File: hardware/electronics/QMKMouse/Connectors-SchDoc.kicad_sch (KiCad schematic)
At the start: 19 parts

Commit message: update schematic from PCB; sync netlist and fix some symbol orientations; also fix LED symbol
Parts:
- USB.C.19, USB.FB.1, USB.FB.2, USB.FB.3, USB.FB.4, USB.FB.5, USB.R.10, USB.R.11, USB.R.12, USB.R.13, USB.R.14, USB.R.15, USB.R.6, USB.R.7, USB.R.8, USB.R.9: footprint (none) -> Chip_Passives.PcbLib:0805
- USB.J.2: footprint (none) -> Connectors.PcbLib:SJ-43514-SMT-TR
- USB.J.3: footprint (none) -> Connectors.PcbLib:DX07S016JA1R1500
- USB.Z.1: footprint (none) -> Diodes.PcbLib:PESD3V3S4UD - SOT95P275X110-6N
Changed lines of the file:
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@@
     (property "Reference" "USB.FB.1" (id 0) (at 186.6392 82.55 90))
     (property "Value" "ACML-0805-601-T" (id 1) (at 186.6392 85.09 90))
-    (property "Footprint" "" (id 2) (at 186.69 91.948 90)
+    (property "Footprint" "Chip_Passives.PcbLib:0805" (id 2) (at 186.69 91.948 90)
       (effects (font (size 1.27 1.27)) hide)
     )
@@
     (property "Reference" "USB.FB.5" (id 0) (at 186.6392 49.53 90))
     (property "Value" "ACML-0805-601-T" (id 1) (at 186.6392 52.07 90))
-    (property "Footprint" "" (id 2) (at 186.69 58.928 90)
+    (property "Footprint" "Chip_Passives.PcbLib:0805" (id 2) (at 186.69 58.928 90)
       (effects (font (size 1.27 1.27)) hide)
     )
@@
       (effects (font (size 1.27 1.27)) (justify left))
     )
-    (property "Footprint" "" (id 2) (at 85.598 35.56 90)
+    (property "Footprint" "Chip_Passives.PcbLib:0805" (id 2) (at 85.598 35.56 90)
       (effects (font (size 1.27 1.27)) hide)
     )
@@
       (effects (font (size 1.27 1.27)) (justify left))
     )
-    (property "Footprint" "" (id 2) (at 229.87 58.928 90)
+    (property "Footprint" "Chip_Passives.PcbLib:0805" (id 2) (at 229.87 58.928 90)
       (effects (font (size 1.27 1.27)) hide)
     )
@@
       (effects (font (size 1.27 1.27)) (justify left))
     )
-    (property "Footprint" "" (id 2) (at 67.818 120.65 90)
+    (property "Footprint" "Chip_Passives.PcbLib:0805" (id 2) (at 67.818 120.65 90)
       (effects (font (size 1.27 1.27)) hide)
     )
@@
       (effects (font (size 1.27 1.27)) (justify left))
     )
-    (property "Footprint" "" (id 2) (at 95.758 120.65 90)
+    (property "Footprint" "Chip_Passives.PcbLib:0805" (id 2) (at 95.758 120.65 90)
       (effects (font (size 1.27 1.27)) hide)
     )
@@
       (effects (font (size 1.27 1.27)) (justify left))
     )
-    (property "Footprint" "" (id 2) (at 103.378 35.56 90)
+    (property "Footprint" "Chip_Passives.PcbLib:0805" (id 2) (at 103.378 35.56 90)
       (effects (font (size 1.27 1.27)) hide)
     )
@@
     (property "Reference" "USB.FB.2" (id 0) (at 186.6392 102.87 90))
     (property "Value" "ACML-0805-601-T" (id 1) (at 186.6392 105.41 90))
-    (property "Footprint" "" (id 2) (at 186.69 112.268 90)
+    (property "Footprint" "Chip_Passives.PcbLib:0805" (id 2) (at 186.69 112.268 90)
       (effects (font (size 1.27 1.27)) hide)
     )
@@
     (property "Reference" "USB.J.2" (id 0) (at 45.72 40.64 0))
     (property "Value" "SJ-43514-SMT-TR" (id 1) (at 43.18 57.15 0))
-    (property "Footprint" "" (id 2) (at 48.26 46.99 0)
+    (property "Footprint" "Connectors.PcbLib:SJ-43514-SMT-TR" (id 2) (at 48.26 46.99 0)
       (effects (font (size 1.27 1.27)) hide)
     )
@@
       (effects (font (size 1.27 1.27)) (justify left))
     )
-    (property "Footprint" "" (id 2) (at 105.918 120.65 90)
+    (property "Footprint" "Chip_Passives.PcbLib:0805" (id 2) (at 105.918 120.65 90)
       (effects (font (size 1.27 1.27)) hide)
     )
@@
       (effects (font (size 1.27 1.27)) (justify right))
     )
-    (property "Footprint" "" (id 2) (at 219.4052 90.17 0)
+    (property "Footprint" "Chip_Passives.PcbLib:0805" (id 2) (at 219.4052 90.17 0)
       (effects (font (size 1.27 1.27)) hide)
     )
@@
       (effects (font (size 1.27 1.27)) (justify right))
     )
-    (property "Footprint" "" (id 2) (at 134.62 146.05 0)
+    (property "Footprint" "Diodes.PcbLib:PESD3V3S4UD - SOT95P275X110-6N" (id 2) (at 134.62 146.05 0)
       (effects (font (size 1.27 1.27)) hide)
     )
@@
     (property "Reference" "USB.FB.4" (id 0) (at 186.6392 36.83 90))
     (property "Value" "ACML-0805-601-T Ferrite Bead 600Ohm" (id 1) (at 186.6392 39.37 90))
-    (property "Footprint" "" (id 2) (at 186.69 46.228 90)
+    (property "Footprint" "Chip_Passives.PcbLib:0805" (id 2) (at 186.69 46.228 90)
       (effects (font (size 1.27 1.27)) hide)
     )
@@
     (property "Reference" "USB.FB.3" (id 0) (at 186.6392 113.03 90))
     (property "Value" "ACML-0805-601-T" (id 1) (at 186.6392 115.57 90))
-    (property "Footprint" "" (id 2) (at 186.69 122.428 90)
+    (property "Footprint" "Chip_Passives.PcbLib:0805" (id 2) (at 186.69 122.428 90)
       (effects (font (size 1.27 1.27)) hide)
     )
@@
       (effects (font (size 1.27 1.27)) (justify left))
     )
-    (property "Footprint" "" (id 2) (at 229.87 112.268 90)
+    (property "Footprint" "Chip_Passives.PcbLib:0805" (id 2) (at 229.87 112.268 90)
       (effects (font (size 1.27 1.27)) hide)
     )
@@
       (effects (font (size 1.27 1.27)) (justify left))
     )
-    (property "Footprint" "" (id 2) (at 77.978 120.65 90)
+    (property "Footprint" "Chip_Passives.PcbLib:0805" (id 2) (at 77.978 120.65 90)
       (effects (font (size 1.27 1.27)) hide)
     )
@@
     (property "Reference" "USB.J.3" (id 0) (at 30.48 80.01 0))
     (property "Value" "DX07S016JA1R1500" (id 1) (at 30.48 82.55 0))
-    (property "Footprint" "" (id 2) (at 34.29 102.87 0)
+    (property "Footprint" "Connectors.PcbLib:DX07S016JA1R1500" (id 2) (at 34.29 102.87 0)
       (effects (font (size 1.27 1.27)) hide)
     )
@@
       (effects (font (size 1.27 1.27)) (justify left))
     )
-    (property "Footprint" "" (id 2) (at 229.87 122.428 90)
+    (property "Footprint" "Chip_Passives.PcbLib:0805" (id 2) (at 229.87 122.428 90)
       (effects (font (size 1.27 1.27)) hide)
     )
@@
       (effects (font (size 1.27 1.27)) (justify left))
     )
-    (property "Footprint" "" (id 2) (at 229.87 46.228 90)
-      (effects (font (size 1.27 1.27)) hide)
-    )
+    (property "Footprint" "Chip_Passives.PcbLib:0805" (id 2) (at 229.87 46.228 90)
+      (effects (font (size 1.27 1.27)) hide)
+    )

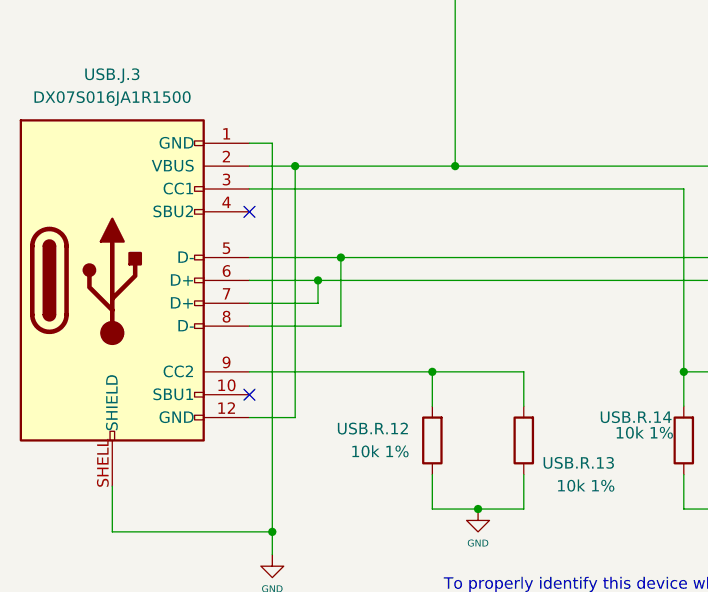
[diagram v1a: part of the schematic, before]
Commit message: Fix all remaining DRC errors and schematic mismatches
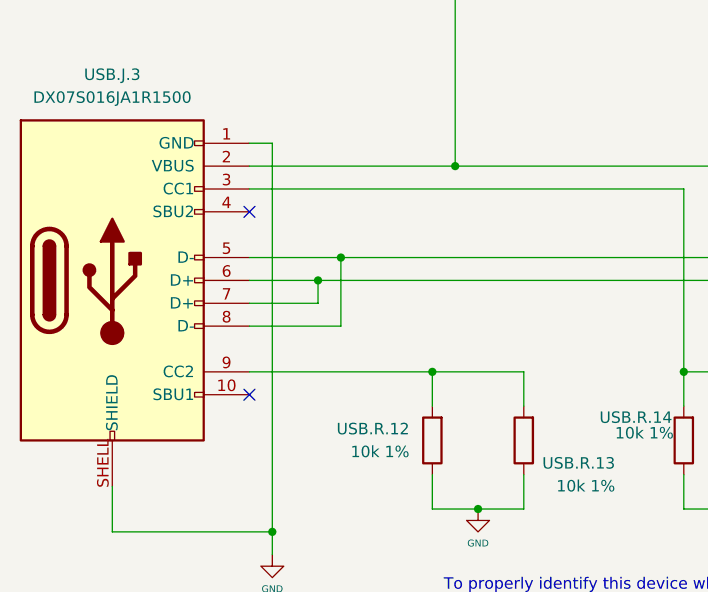
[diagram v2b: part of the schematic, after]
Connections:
- net GND: now also USB.J.3.12 (GND)
- net at USB.FB.1.1, USB.J.2.1 (S), USB.J.3.2 (VBUS)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: now also USB.J.3.11 (VBUS); no longer USB.J.3.12 (GND)
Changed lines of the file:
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@@
   (junction (at 68.58 90.17) (diameter 0) (color 0 0 0 0)
-  )
-  (junction (at 50.8 90.17) (diameter 0) (color 0 0 0 0)
   )
   (junction (at 99.06 128.27) (diameter 0) (color 0 0 0 0)
@@
     (stroke (width 0) (type default) (color 0 0 0 0))
   )
+  (wire (pts (xy 48.26 87.63) (xy 48.26 130.81))
+    (stroke (width 0) (type default) (color 0 0 0 0))
+  )
   (wire (pts (xy 104.14 116.84) (xy 104.14 113.03))
     (stroke (width 0) (type default) (color 0 0 0 0))
@@
     (stroke (width 0) (type default) (color 0 0 0 0))
   )
-  (wire (pts (xy 50.8 90.17) (xy 50.8 118.11))
-    (stroke (width 0) (type default) (color 0 0 0 0))
-  )
   (wire (pts (xy 68.58 44.45) (xy 53.34 44.45))
     (stroke (width 0) (type default) (color 0 0 0 0))
@@
     (stroke (width 0) (type default) (color 0 0 0 0))
   )
-  (wire (pts (xy 50.8 90.17) (xy 45.72 90.17))
-    (stroke (width 0) (type default) (color 0 0 0 0))
-  )
   (wire (pts (xy 167.64 166.37) (xy 167.64 113.03))
     (stroke (width 0) (type default) (color 0 0 0 0))
@@
     (stroke (width 0) (type default) (color 0 0 0 0))
   )
-  (wire (pts (xy 68.58 90.17) (xy 50.8 90.17))
+  (wire (pts (xy 45.72 90.17) (xy 68.58 90.17))
     (stroke (width 0) (type default) (color 0 0 0 0))
   )
@@
     (stroke (width 0) (type default) (color 0 0 0 0))
   )
-  (wire (pts (xy 48.26 87.63) (xy 48.26 130.81))
-    (stroke (width 0) (type default) (color 0 0 0 0))
-  )
   (wire (pts (xy 71.12 128.27) (xy 66.04 128.27))
     (stroke (width 0) (type default) (color 0 0 0 0))
@@
   )
   (wire (pts (xy 149.86 44.45) (xy 182.88 44.45))
-    (stroke (width 0) (type default) (color 0 0 0 0))
-  )
-  (wire (pts (xy 50.8 118.11) (xy 45.72 118.11))
     (stroke (width 0) (type default) (color 0 0 0 0))
   )
@@
     (pin "1")
     (pin "10")
+    (pin "11")
     (pin "12")
     (pin "2")

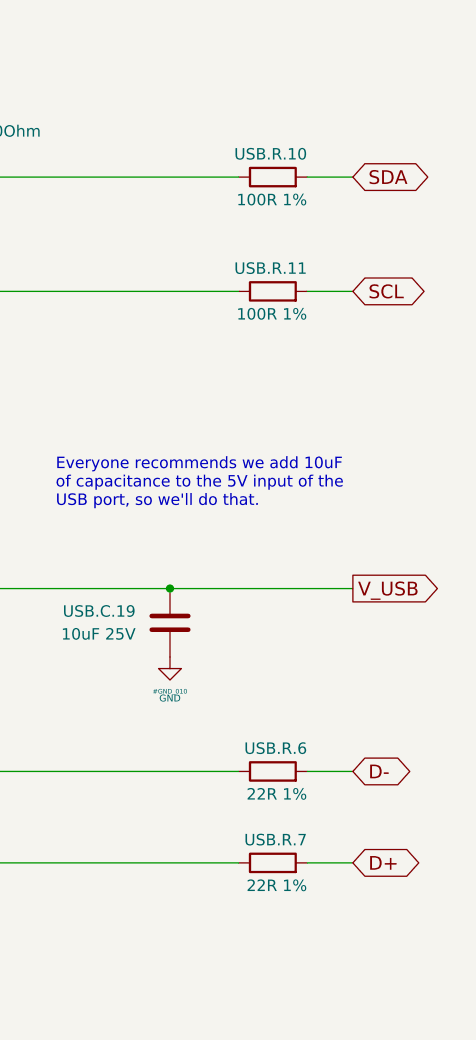
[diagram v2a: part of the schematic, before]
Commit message: fix ERC errors and use hierarchy labels
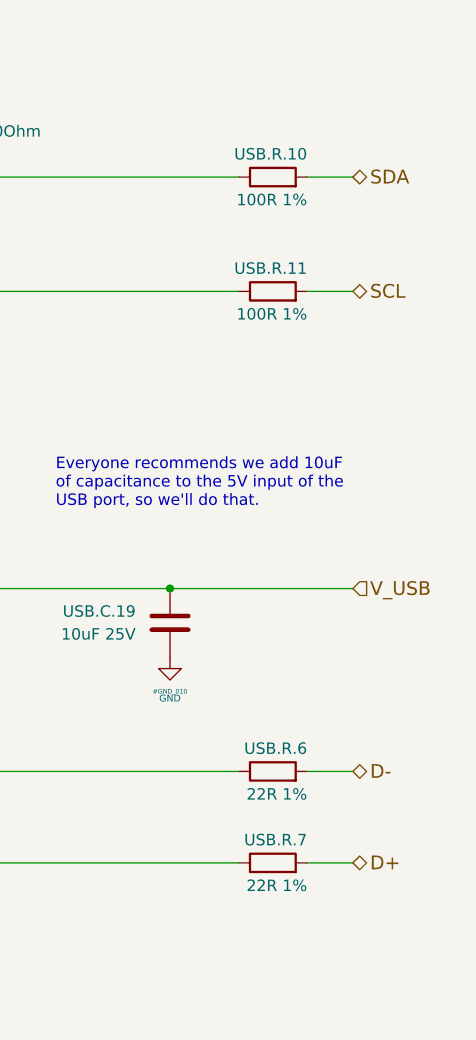
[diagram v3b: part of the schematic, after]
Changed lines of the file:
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@@
     (effects (font (size 1.27 1.27)) (justify left bottom))
   )
-  (global_label "D-" (shape bidirectional) (at 238.76 110.49 0) (fields_autoplaced)
+  (hierarchical_label "V_USB" (shape input) (at 238.76 90.17 0)
     (effects (font (size 1.524 1.524)) (justify left))
-    (property "Intersheet References" "${INTERSHEET_REFS}" (id 0) (at -7.62 -62.23 0)
-      (effects (font (size 1.27 1.27)) hide)
-    )
   )
-  (global_label "SDA" (shape bidirectional) (at 238.76 44.45 0) (fields_autoplaced)
+  (hierarchical_label "D-" (shape bidirectional) (at 238.76 110.49 0)
     (effects (font (size 1.524 1.524)) (justify left))
-    (property "Intersheet References" "${INTERSHEET_REFS}" (id 0) (at -7.62 -62.23 0)
-      (effects (font (size 1.27 1.27)) hide)
-    )
   )
-  (global_label "D+" (shape bidirectional) (at 238.76 120.65 0) (fields_autoplaced)
+  (hierarchical_label "D+" (shape bidirectional) (at 238.76 120.65 0)
     (effects (font (size 1.524 1.524)) (justify left))
-    (property "Intersheet References" "${INTERSHEET_REFS}" (id 0) (at -7.62 -62.23 0)
-      (effects (font (size 1.27 1.27)) hide)
-    )
   )
-  (global_label "V_USB" (shape output) (at 238.76 90.17 0) (fields_autoplaced)
+  (hierarchical_label "SCL" (shape bidirectional) (at 238.76 57.15 0)
     (effects (font (size 1.524 1.524)) (justify left))
-    (property "Intersheet References" "${INTERSHEET_REFS}" (id 0) (at -7.62 -62.23 0)
-      (effects (font (size 1.27 1.27)) hide)
-    )
   )
-  (global_label "SCL" (shape bidirectional) (at 238.76 57.15 0) (fields_autoplaced)
+  (hierarchical_label "SDA" (shape bidirectional) (at 238.76 44.45 0)
     (effects (font (size 1.524 1.524)) (justify left))
-    (property "Intersheet References" "${INTERSHEET_REFS}" (id 0) (at -7.62 -62.23 0)
-      (effects (font (size 1.27 1.27)) hide)
-    )
   )
   (symbol (lib_id "power:GND") (at 63.5 62.23 0) (unit 1)

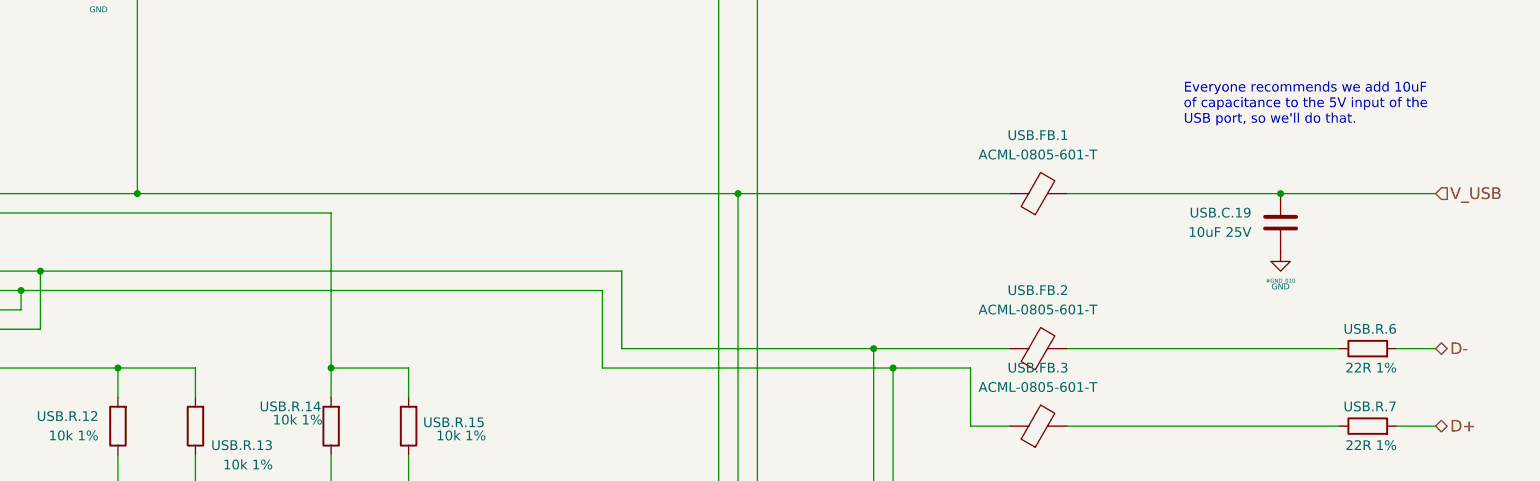
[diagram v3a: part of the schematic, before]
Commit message: Fix all ERC errors and replot the schematic
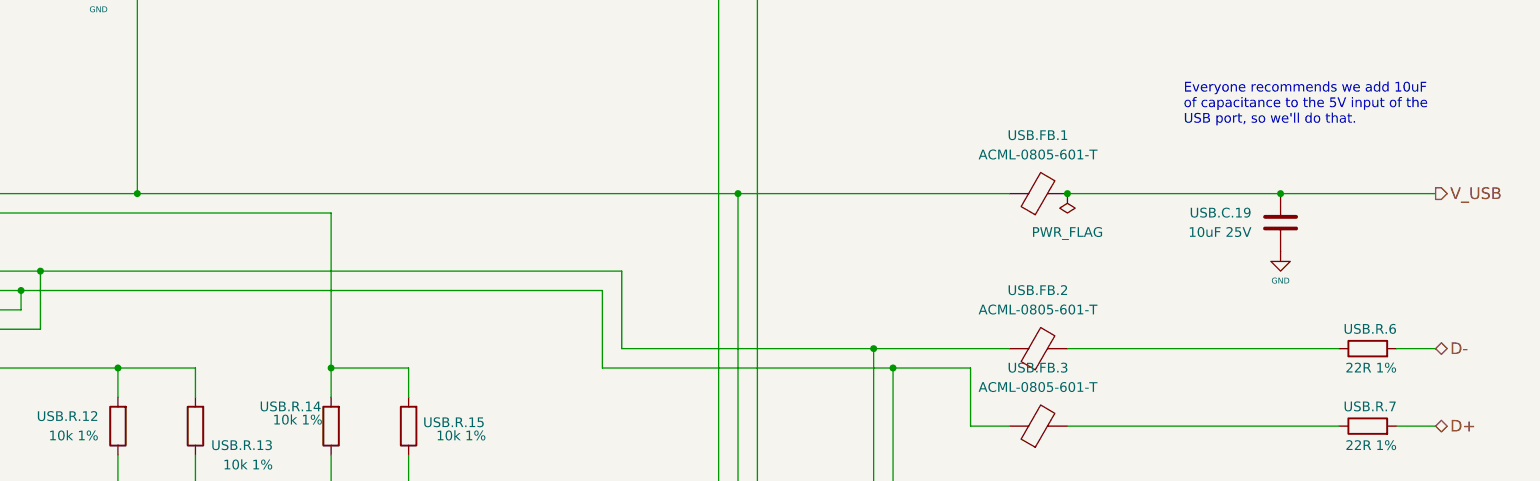
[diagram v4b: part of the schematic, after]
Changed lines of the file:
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@@
   (junction (at 93.98 113.03) (diameter 0) (color 0 0 0 0)
+  )
+  (junction (at 190.5 90.17) (diameter 0) (color 0 0 0 0)
   )
   (junction (at 167.64 113.03) (diameter 0) (color 0 0 0 0)
@@
     (stroke (width 0) (type default) (color 0 0 0 0))
   )
-  (wire (pts (xy 147.32 90.17) (xy 68.58 90.17))
-    (stroke (width 0) (type default) (color 0 0 0 0))
-  )
   (wire (pts (xy 101.6 49.53) (xy 101.6 39.37))
     (stroke (width 0) (type default) (color 0 0 0 0))
@@
     (stroke (width 0) (type default) (color 0 0 0 0))
   )
+  (wire (pts (xy 68.58 90.17) (xy 147.32 90.17))
+    (stroke (width 0) (type default) (color 0 0 0 0))
+  )
   (wire (pts (xy 165.1 156.21) (xy 165.1 110.49))
     (stroke (width 0) (type default) (color 0 0 0 0))
@@
     (stroke (width 0) (type default) (color 0 0 0 0))
   )
-  (wire (pts (xy 182.88 90.17) (xy 147.32 90.17))
-    (stroke (width 0) (type default) (color 0 0 0 0))
-  )
   (wire (pts (xy 226.06 44.45) (xy 190.5 44.45))
     (stroke (width 0) (type default) (color 0 0 0 0))
@@
   )
   (wire (pts (xy 76.2 124.46) (xy 76.2 128.27))
+    (stroke (width 0) (type default) (color 0 0 0 0))
+  )
+  (wire (pts (xy 147.32 90.17) (xy 182.88 90.17))
     (stroke (width 0) (type default) (color 0 0 0 0))
   )
@@
     (effects (font (size 1.27 1.27)) (justify left bottom))
   )
-  (hierarchical_label "V_USB" (shape input) (at 238.76 90.17 0)
+  (hierarchical_label "V_USB" (shape output) (at 238.76 90.17 0)
     (effects (font (size 1.524 1.524)) (justify left))
   )
@@
     (in_bom yes) (on_board yes)
     (property "Reference" "#GND_010" (id 0) (at 218.44 101.6 0)
-      (effects (font (size 0.508 0.508)))
-    )
-    (property "Value" "GND" (id 1) (at 218.44 102.362 0)
+      (effects (font (size 0.508 0.508)) hide)
+    )
+    (property "Value" "GND" (id 1) (at 218.44 101.6 0)
       (effects (font (size 0.762 0.762)))
     )
@@
     (pin "2")
   )
+  (symbol (lib_id "power:PWR_FLAG") (at 190.5 90.17 180) (unit 1)
+    (in_bom yes) (on_board yes) (fields_autoplaced)
+    (property "Reference" "#FLG0101" (id 0) (at 190.5 92.075 0)
+      (effects (font (size 1.27 1.27)) hide)
+    )
+    (property "Value" "PWR_FLAG" (id 1) (at 190.5 95.25 0))
+    (property "Footprint" "" (id 2) (at 190.5 90.17 0)
+      (effects (font (size 1.27 1.27)) hide)
+    )
+    (property "Datasheet" "~" (id 3) (at 190.5 90.17 0)
+      (effects (font (size 1.27 1.27)) hide)
+    )
+    (pin "1")
+  )
   (symbol (lib_id "Mouse_Parts:AudioJack4") (at 48.26 46.99 0) (unit 1)
